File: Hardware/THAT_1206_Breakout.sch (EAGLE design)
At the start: 23 parts, among them IC1 THAT1206, J1 INPUT, J3 CHASSIS

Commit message: Routed PCB.
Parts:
- removed H5, H6, H7, H8: STAND-OFF, SparkFun-Electromechanical:STAND-OFF
- added FD1, FD2: FIDUCIALUFIDUCIAL, SparkFun-Aesthetics:FIDUCIALUFIDUCIAL
- added LOGO1: SFE_LOGO_NAME.1_INCH, SparkFun-Aesthetics:SFE_LOGO_NAME.1_INCH
- added LOGO2, LOGO5: OSHW-LOGOS, SparkFun-Aesthetics:OSHW-LOGOS
- added LOGO4: SFE_LOGO_FLAME.2_INCH, SparkFun-Aesthetics:SFE_LOGO_FLAME.2_INCH
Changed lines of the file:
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@@
 <part name="SUPPLY7" library="SparkFun-Aesthetics" deviceset="VNEG" device=""/>
 <part name="SUPPLY8" library="SparkFun-Aesthetics" deviceset="VCC" device=""/>
-<part name="H5" library="SparkFun-Electromechanical" deviceset="STAND-OFF" device=""/>
-<part name="H6" library="SparkFun-Electromechanical" deviceset="STAND-OFF" device=""/>
-<part name="H7" library="SparkFun-Electromechanical" deviceset="STAND-OFF" device=""/>
-<part name="H8" library="SparkFun-Electromechanical" deviceset="STAND-OFF" device=""/>
 <part name="D5" library="SparkFun-DiscreteSemi" deviceset="BAV99" device=""/>
 <part name="D6" library="SparkFun-DiscreteSemi" deviceset="BAV99" device=""/>
@@
 <part name="D3" library="that-ics" deviceset="12V-ZENER-DIODE" device="" value="12V"/>
 <part name="D4" library="that-ics" deviceset="12V-ZENER-DIODE" device="" value="12V"/>
+<part name="LOGO1" library="SparkFun-Aesthetics" deviceset="SFE_LOGO_NAME" device=".1_INCH"/>
+<part name="LOGO2" library="SparkFun-Aesthetics" deviceset="OSHW-LOGO" device="S"/>
+<part name="LOGO4" library="SparkFun-Aesthetics" deviceset="SFE_LOGO_FLAME" device=".2_INCH" value="SFE_LOGO_FLAME.2_INCH"/>
+<part name="LOGO5" library="SparkFun-Aesthetics" deviceset="OSHW-LOGO" device="S"/>
+<part name="FD1" library="SparkFun-Aesthetics" deviceset="FIDUCIAL" device="UFIDUCIAL"/>
+<part name="FD2" library="SparkFun-Aesthetics" deviceset="FIDUCIAL" device="UFIDUCIAL"/>
 </parts>
 <sheets>
@@
 <instance part="SUPPLY7" gate="G$2" x="182.88" y="81.28"/>
 <instance part="SUPPLY8" gate="G$1" x="190.5" y="104.14"/>
-<instance part="H5" gate="G$1" x="233.68" y="33.02"/>
-<instance part="H6" gate="G$1" x="233.68" y="30.48"/>
-<instance part="H7" gate="G$1" x="236.22" y="33.02"/>
-<instance part="H8" gate="G$1" x="236.22" y="30.48"/>
 <instance part="D5" gate="G$1" x="134.62" y="134.62"/>
 <instance part="D6" gate="G$1" x="116.84" y="124.46"/>
@@
 <instance part="D3" gate="G$1" x="88.9" y="124.46" rot="R180"/>
 <instance part="D4" gate="G$1" x="160.02" y="134.62" rot="R180"/>
+<instance part="LOGO1" gate="G$1" x="185.42" y="35.56"/>
+<instance part="LOGO2" gate="G$1" x="172.72" y="45.72"/>
+<instance part="LOGO4" gate="G$1" x="149.86" y="35.56"/>
+<instance part="LOGO5" gate="G$1" x="172.72" y="45.72"/>
+<instance part="FD1" gate="G$1" x="246.38" y="20.32"/>
+<instance part="FD2" gate="G$1" x="246.38" y="17.78"/>
 </instances>
 <busses>

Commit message: After proto review.
Many fit & finish changes.
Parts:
- removed D5: (no value), SparkFun-DiscreteSemi:BAV99
- added D1: 12V, that-ics:12V-ZENER-DIODE
- added FD3, FD4: FIDUCIALUFIDUCIAL, SparkFun-Aesthetics:FIDUCIALUFIDUCIAL
- added J2: INPUT, SparkFun-Connectors:AUDIO-JACK4-.25-HORIZ-TRS
- added J5: TN, SparkFun-Connectors:M01PTH_NO_SILK_YES_STOP
- added J6: SN, SparkFun-Connectors:M01PTH_NO_SILK_YES_STOP
- added LOGO3: OSHW-LOGOS, SparkFun-Aesthetics:OSHW-LOGOS
- C4: value 0.1uF -> 220uf; device SparkFun-Capacitors:0.1UF-25V-5%(0603) -> that-ics:PANA-EEE-FKOJ221P
- C6: value 220uf -> 0.1uF; device that-ics:PANA-EEE-FKOJ221P -> SparkFun-Capacitors:0.1UF-25V-5%(0603)
- D2: value (none) -> BAV99
- D3: value 12V -> BAV99; device that-ics:12V-ZENER-DIODE -> SparkFun-DiscreteSemi:BAV99
- J1: value INPUT -> CHASSIS; device SparkFun-Connectors:AUDIO-JACK4-.25-HORIZ-TRS -> SparkFun-Connectors:M021X02_NO_SILK
- J3: value CHASSIS -> (none); device SparkFun-Connectors:M021X02_NO_SILK -> SparkFun-Connectors:M04NO_SILK_ALL_ROUND
- J4: value (none) -> RN; device SparkFun-Connectors:M04NO_SILK_ALL_ROUND -> SparkFun-Connectors:M01PTH_NO_SILK_YES_STOP
- LOGO1: value SFE_LOGO_NAME.1_INCH -> SFE_LOGO_FLAME.2_INCH; device SparkFun-Aesthetics:SFE_LOGO_NAME.1_INCH -> SparkFun-Aesthetics:SFE_LOGO_FLAME.2_INCH
- LOGO4: value SFE_LOGO_FLAME.2_INCH -> SFE_LOGO_NAME.1_INCH; device SparkFun-Aesthetics:SFE_LOGO_FLAME.2_INCH -> SparkFun-Aesthetics:SFE_LOGO_NAME.1_INCH
- LOGO5: value OSHW-LOGOS -> SFE_LOGO_FLAME.2_INCH; device SparkFun-Aesthetics:OSHW-LOGOS -> SparkFun-Aesthetics:SFE_LOGO_FLAME.2_INCH
- renumbered D6 to D2
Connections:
- new net N$10: J2.RING-NORM, J4.1
- new net N$8: J2.EARTH-NORM, J6.1
- new net N$9: J2.TIP-NORM, J5.1
- net GND: now also C6.2, J3.1; no longer C4.2, J4.1
- net GND-ISO: now also J1.1, J1.2, J2.EARTH; no longer J1.EARTH, J3.1, J3.2
- net N$1: now also J2.RING, R1.1; no longer J1.RING, R2.1
- net N$12: now also D1.A, D3.A1; no longer D3.A, D5.A1
- net N$15: now also D3.C2; no longer D5.C2
- net N$2: now also D3.COM, R1.2; no longer D5.COM, R2.2
- net N$3: now also J2.TIP, R2.1; no longer J1.TIP, R1.1
- net N$4: now also R2.2; no longer R1.2
- net N$6: now also C4.-; no longer C6.-
- net N$7: now also C4.+; no longer C6.+
- net RCV: now also J3.4; no longer J4.4
- net VCC: now also C5.1, J3.3; no longer C4.1, J4.3
- net VNEG: now also C6.1, D1.C, J3.2; no longer C5.1, D3.C, J4.2
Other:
- note added: "D1, D2, D3, D4 form extended range clamp, holding input to 12V beyond the supply rails. The max Vin range published for the IC is +/-31V."
- note added: "J4, J5, J6 are normals of TRS connections. If jack is not present, they connect to their respective T/R/S connections. If jack is present, they float."
- moved on the sheet: C5, R1, R2

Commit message: Ran engineering checklist, a few small changes.
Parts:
- J1: value CHASSIS -> INPUT; device SparkFun-Connectors:M021X02_NO_SILK -> SparkFun-Connectors:AUDIO-JACK4-.25-HORIZ-TRS
- J2: value INPUT -> CHASSIS; device SparkFun-Connectors:AUDIO-JACK4-.25-HORIZ-TRS -> SparkFun-Connectors:M021X02_NO_SILK
- J3: value (none) -> RN; device SparkFun-Connectors:M04NO_SILK_ALL_ROUND -> SparkFun-Connectors:M01PTH_NO_SILK_YES_STOP
- J4: value RN -> TN
- J5: value TN -> SN
- J6: value SN -> 1x4; device SparkFun-Connectors:M01PTH_NO_SILK_YES_STOP -> SparkFun-Connectors:M04NO_SILK_ALL_ROUND
- LOGO2: value OSHW-LOGOS -> SFE_LOGO_FLAME.2_INCH; device SparkFun-Aesthetics:OSHW-LOGOS -> SparkFun-Aesthetics:SFE_LOGO_FLAME.2_INCH
- LOGO4: value SFE_LOGO_NAME.1_INCH -> OSHW-LOGOS; device SparkFun-Aesthetics:SFE_LOGO_NAME.1_INCH -> SparkFun-Aesthetics:OSHW-LOGOS
- LOGO5: value SFE_LOGO_FLAME.2_INCH -> SFE_LOGO_NAME.1_INCH; device SparkFun-Aesthetics:SFE_LOGO_FLAME.2_INCH -> SparkFun-Aesthetics:SFE_LOGO_NAME.1_INCH
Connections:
- net GND: now also J6.1; no longer J3.1
- net GND-ISO: now also J1.EARTH, J2.1, J2.2; no longer J1.1, J1.2, J2.EARTH
- net N$1: now also J1.RING; no longer J2.RING
- net N$10: now also J1.RING-NORM, J3.1; no longer J2.RING-NORM, J4.1
- net N$3: now also J1.TIP; no longer J2.TIP
- net N$8: now also J1.EARTH-NORM, J5.1; no longer J2.EARTH-NORM, J6.1
- net N$9: now also J1.TIP-NORM, J4.1; no longer J2.TIP-NORM, J5.1
- net RCV: now also J6.4; no longer J3.4
- net VCC: now also J6.3; no longer J3.3
- net VNEG: now also J6.2; no longer J3.2
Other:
- moved on the sheet: J4, J5

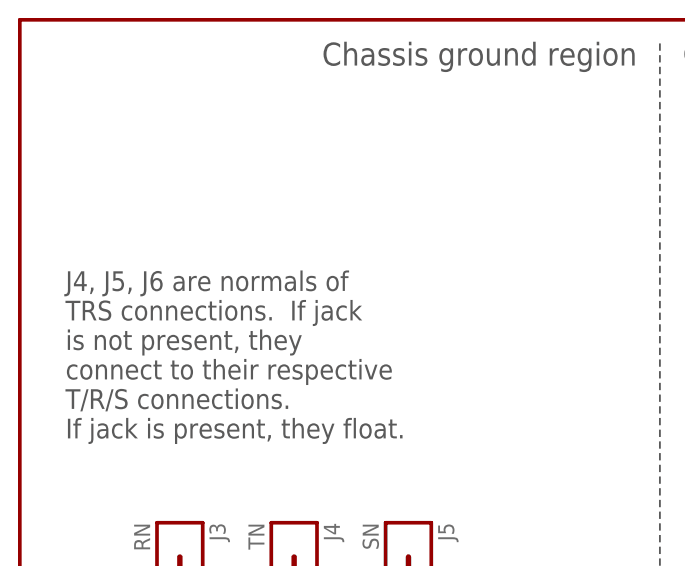
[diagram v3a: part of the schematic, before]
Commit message: Fixing text in schem.
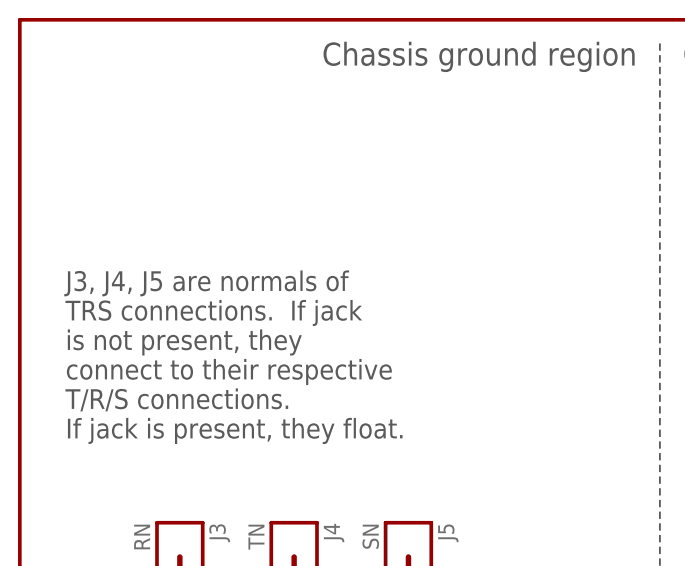
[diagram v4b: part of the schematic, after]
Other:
- note added: "J3, J4, J5 are normals of TRS connections. If jack is not present, they connect to their respective T/R/S connections. If jack is present, they float."
- note removed: "J4, J5, J6 are normals of TRS connections. If jack is not present, they connect to their respective T/R/S connections. If jack is present, they float."
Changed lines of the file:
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@@
 rails.  The max Vin range published for
 the IC is +/-31V.</text>
-<text x="5.08" y="157.48" size="2.1844" layer="97" font="vector" align="top-left">J4, J5, J6 are normals of
+<text x="5.08" y="157.48" size="2.1844" layer="97" font="vector" align="top-left">J3, J4, J5 are normals of
 TRS connections.  If jack
 is not present, they

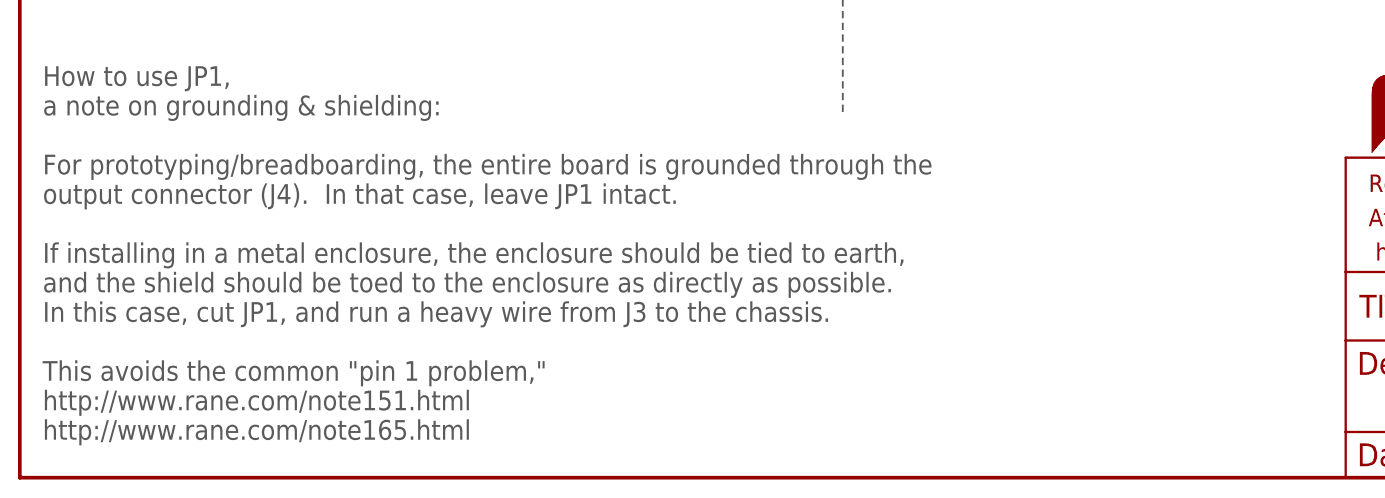
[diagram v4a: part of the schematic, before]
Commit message: Fixing Kade's checklist issues.
-Un-"toed."
-Moved chassis ground connection.
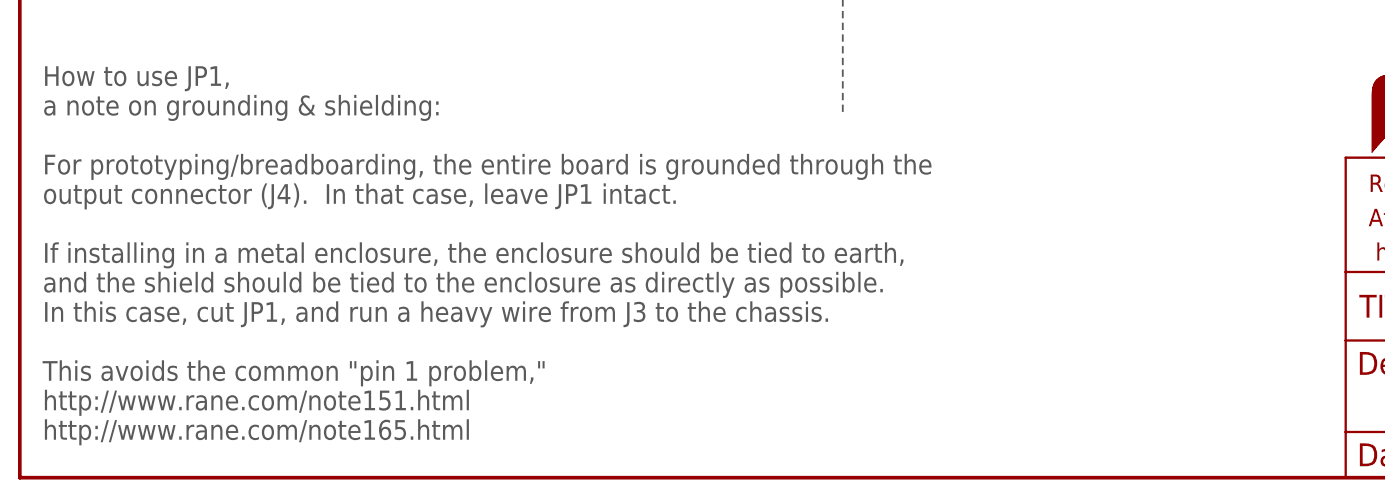
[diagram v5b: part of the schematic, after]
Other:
- note added: "How to use JP1, a note on grounding & shielding: For prototyping/breadboarding, the entire board is grounded through the output connector (J4). In that case, leave JP1 intact. If installing in a metal enclosure, the enclosure should be tied to earth, and the shield should be tied to the enclosure as directly as possible. In this case, cut JP1, and run a heavy wire from J3 to the chassis. This avo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"
- note removed: "How to use JP1, a note on grounding & shielding: For prototyping/breadboarding, the entire board is grounded through the output connector (J4). In that case, leave JP1 intact. If installing in a metal enclosure, the enclosure should be tied to earth, and the shield should be toed to the enclosure as directly as possible. In this case, cut JP1, and run a heavy wire from J3 to the chassis. This avo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"
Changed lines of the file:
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@@
 output connector (J4).  In that case, leave JP1 intact.
 If installing in a metal enclosure, the enclosure should be tied to earth,
-and the shield should be toed to the enclosure as directly as possible.
+and the shield should be tied to the enclosure as directly as possible.
 In this case, cut JP1, and run a heavy wire from J3 to the chassis.
 This avoids the common "pin 1 problem,"

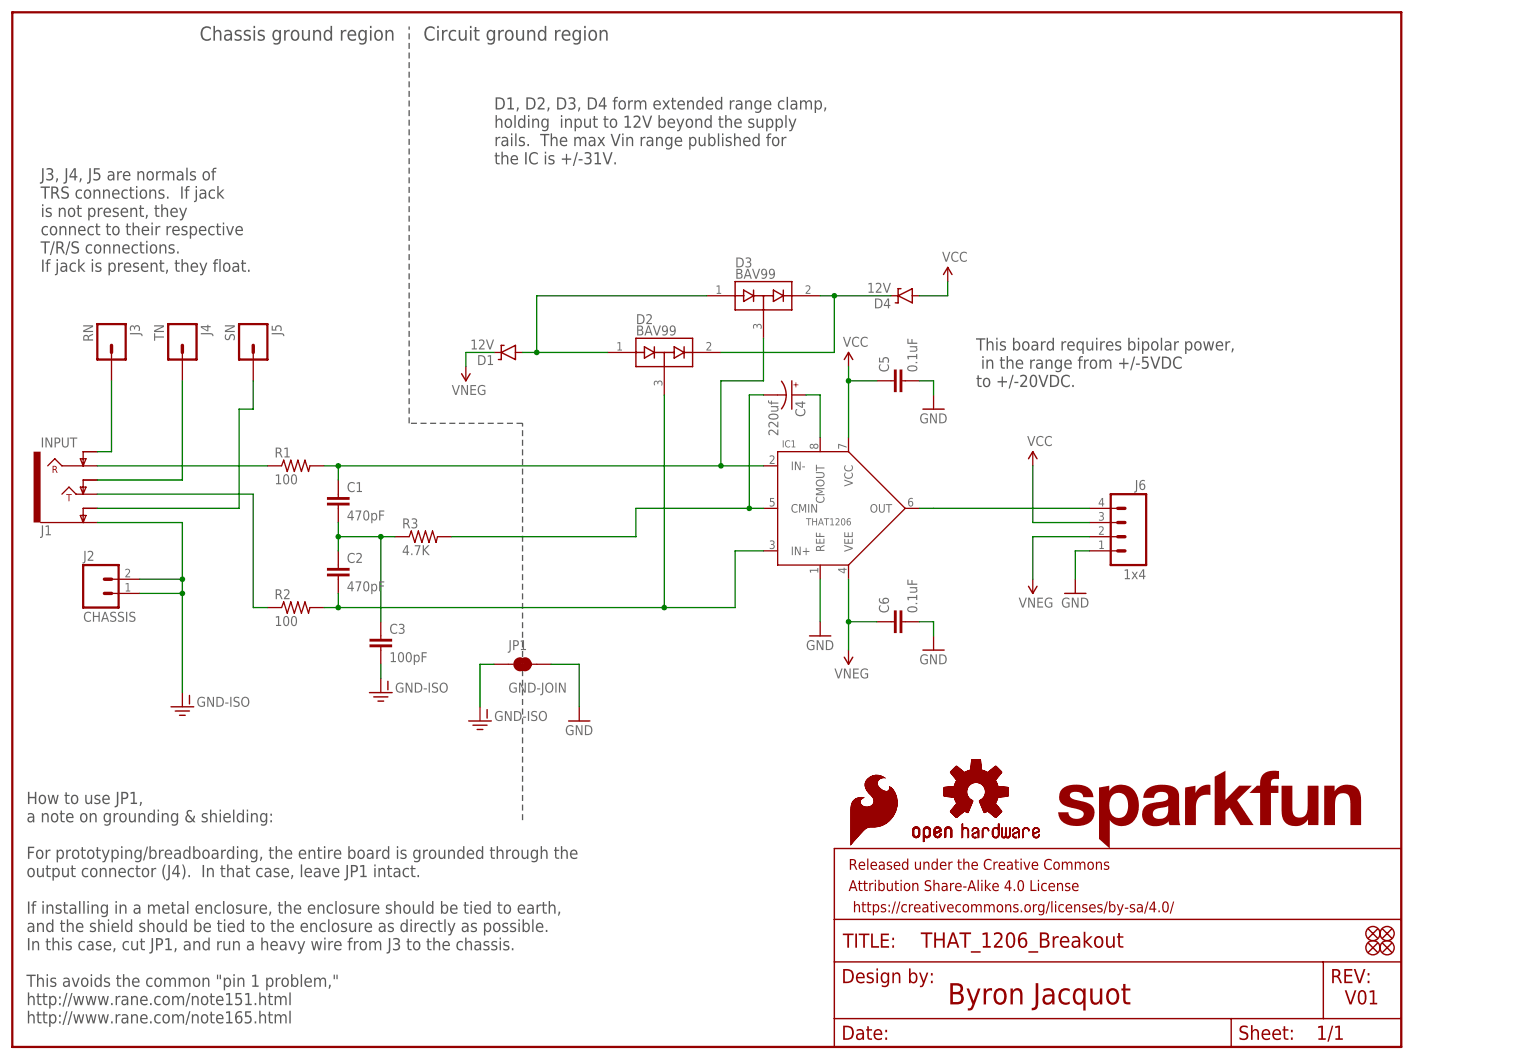
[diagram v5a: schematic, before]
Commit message: Adding testpoints on T/R/S connections.
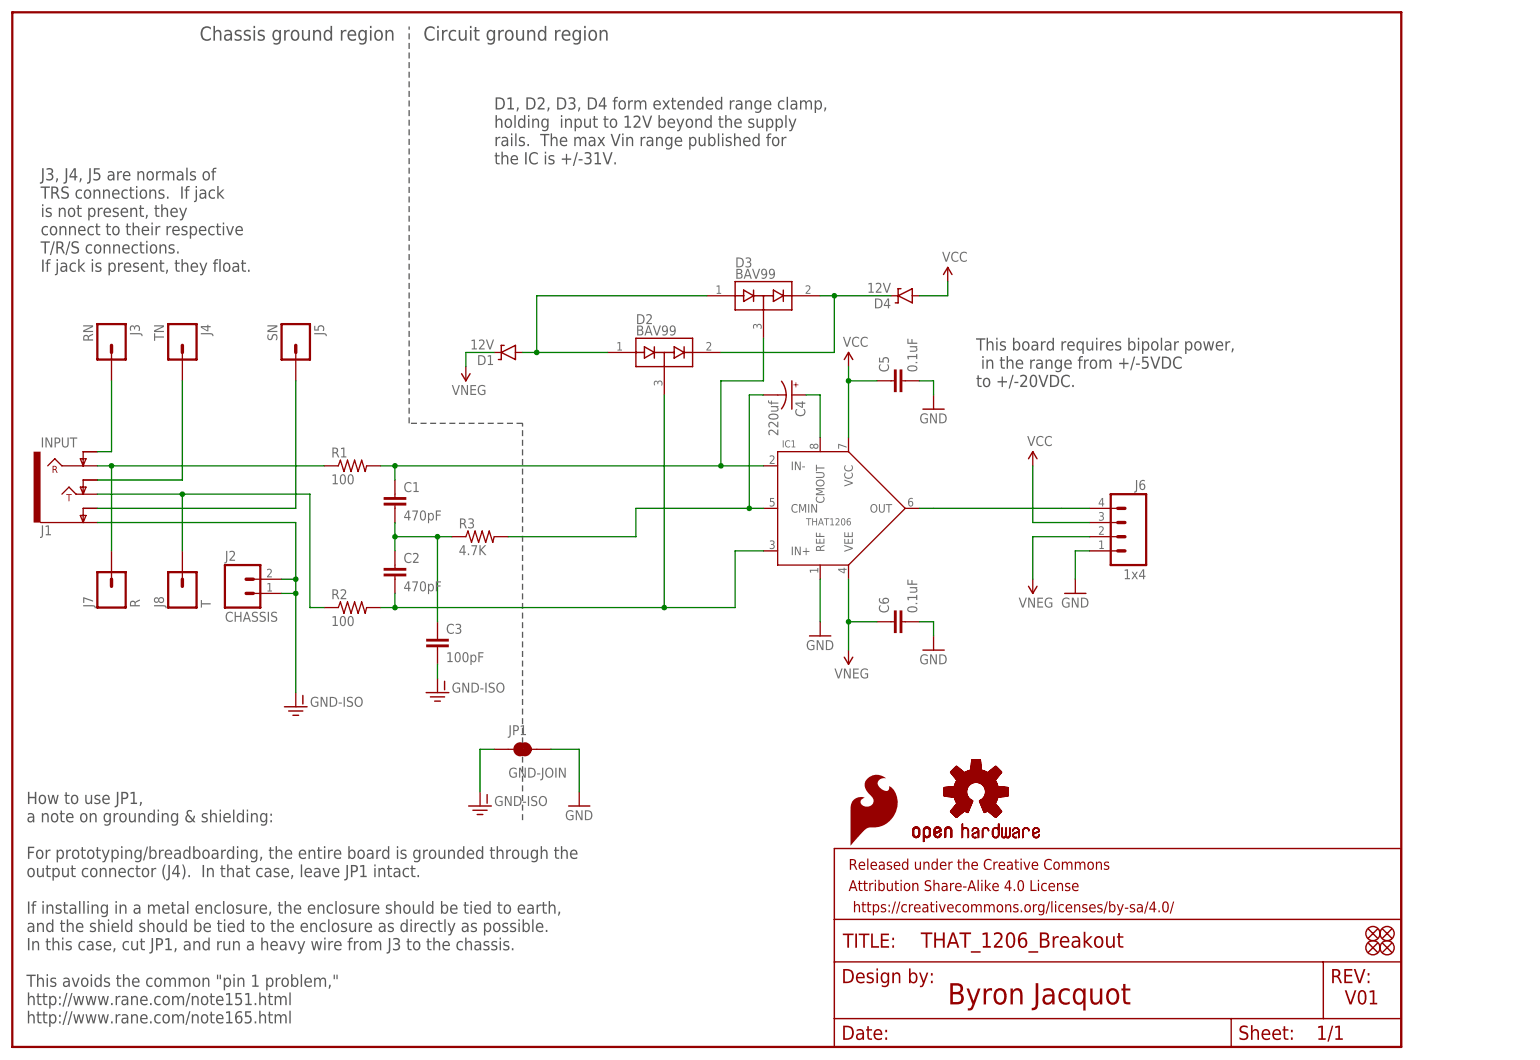
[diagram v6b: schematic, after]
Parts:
- removed LOGO1: SFE_LOGO_FLAME.2_INCH, SparkFun-Aesthetics:SFE_LOGO_FLAME.2_INCH
- removed LOGO5: SFE_LOGO_NAME.1_INCH, SparkFun-Aesthetics:SFE_LOGO_NAME.1_INCH
- added J7: R, SparkFun-Connectors:M01PTH_NO_SILK_YES_STOP
- added J8: T, SparkFun-Connectors:M01PTH_NO_SILK_YES_STOP
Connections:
- net N$1: now also J7.1
- net N$3: now also J8.1
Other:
- moved on the sheet: C1, C2, C3, J2, J5, JP1, R1, R2, R3
